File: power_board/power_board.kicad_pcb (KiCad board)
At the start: 2 copper layers, 171.8 x 117.7 mm, 88 parts, among them J1 PROG, J10 M4, J11 5V_1, J12 M5, J13 M6, J14 M7, J15 FAN, J16 Screw_Terminal_01x02, J17 MB_interface, J18 Conn_01x02_Female, J19 12V_1, J2 M1, J20 12V_2, J21 12V_3, J22 12V_4, J23 48V_1, J24 48V_2, J25 48V_3, J26 48V_4, J27 Screw_Terminal_01x02, J3 M2, J4 Conn_01x02_Female, J5 Conn_01x02_Female, J6 Conn_01x01_Male, J7 Conn_01x01_Male, J8 Screw_Terminal_01x02, J9 M3, Q1 2N3906, SW1 SW_Push, U1 ACS758xCB-050B-PFF, U10 MAX31855KASA, U2 ACS758xCB-050B-PFF, U3 MCP2515-EST, U4 MAX31855KASA, U5 ATA6560,1, U6 BTS50085-1TMA, U7 ATmega328P-AU, U8 BTS50085-1TMA, U9 LM2596S-5, Y1 20Mhz, Y2 16Mhz

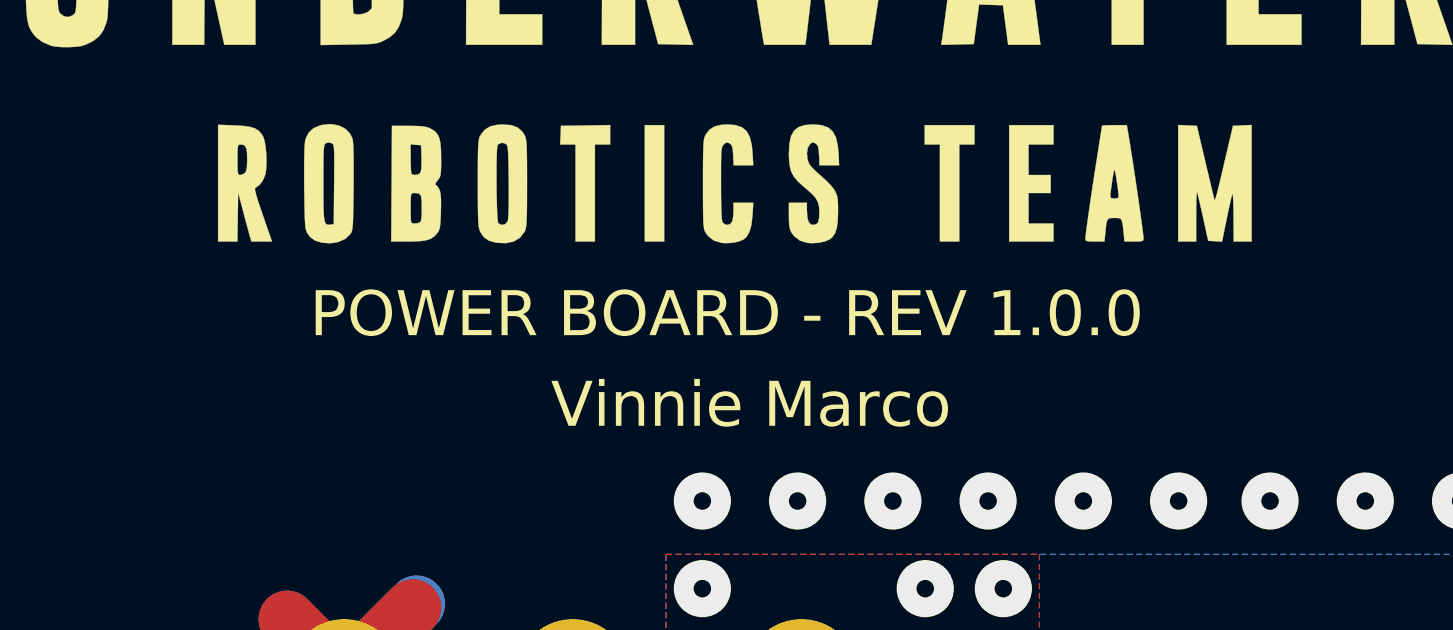
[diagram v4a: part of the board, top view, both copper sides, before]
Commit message: S1.0.0 B1.0.1 Update silkscreen for schematic/pcb version
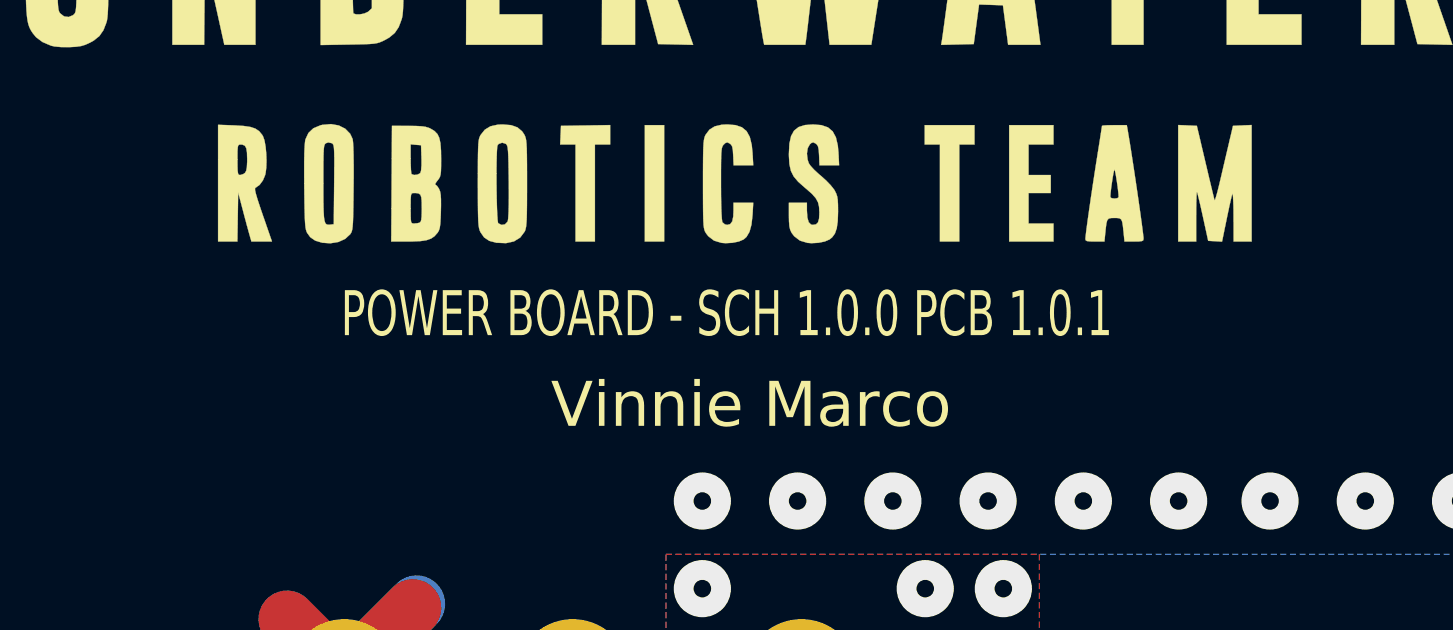
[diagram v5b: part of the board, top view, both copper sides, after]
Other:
- board text added: "POWER BOARD - SCH 1.0.0 PCB 1.0.1"
- board text removed: "POWER BOARD - REV 1.0.0"
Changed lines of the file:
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@@
   )
   (setup
-    (last_trace_width 0.6096)
+    (last_trace_width 0.3048)
     (user_trace_width 0.3048)
     (user_trace_width 0.6096)
@@
       (padsonsilk false)
       (subtractmaskfromsilk false)
-      (outputformat 3)
+      (outputformat 1)
       (mirror false)
       (drillshape 0)
       (scaleselection 1)
-      (outputdirectory "../../../../Desktop/"))
+      (outputdirectory "gerbers_drills/"))
   )
   (net 0 "")
@@
     (effects (font (size 1.5 1.5) (thickness 0.375)))
   )
-  (gr_text "POWER BOARD - REV 1.0.0" (at 157.6578 112.903) (layer F.SilkS)
-    (effects (font (size 1.5 1.5) (thickness 0.375)))
+  (gr_text "POWER BOARD - SCH 1.0.0 PCB 1.0.1" (at 157.6578 112.903) (layer F.SilkS)
+    (effects (font (size 1.5 1) (thickness 0.25)))
   )
   (via (at 152.527 59.563) (size 1.905) (drill 0.5842) (layers F.Cu B.Cu) (net 1))

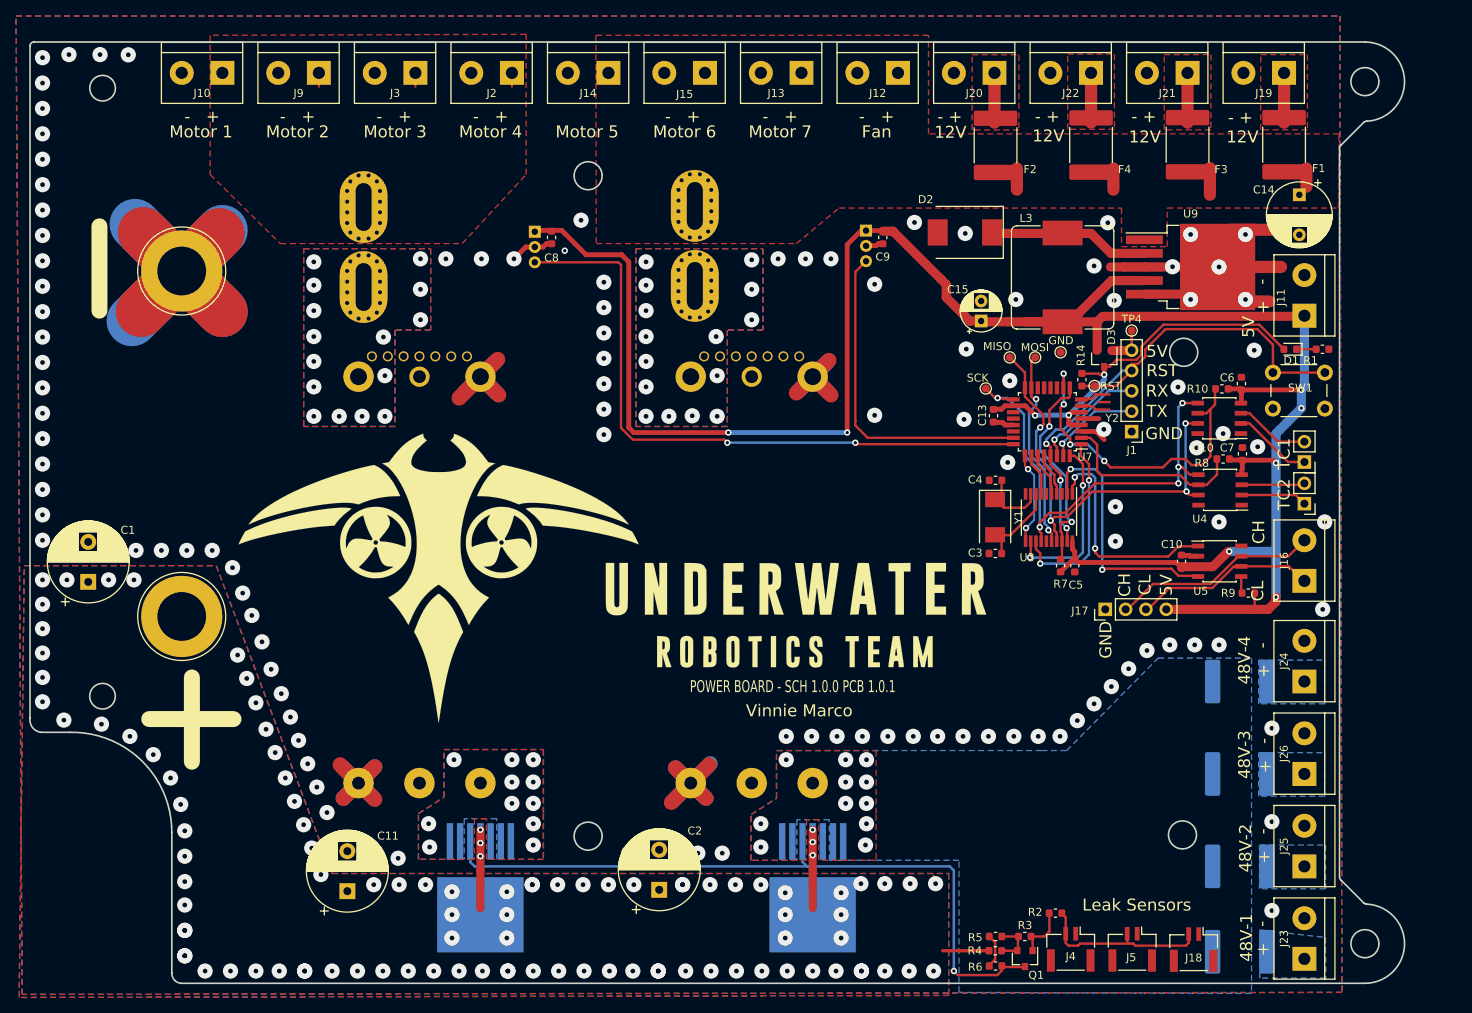
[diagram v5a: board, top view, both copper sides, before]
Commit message: Replaced moutning holes drawn in edge cuts with real holes and regenerated all gerbers
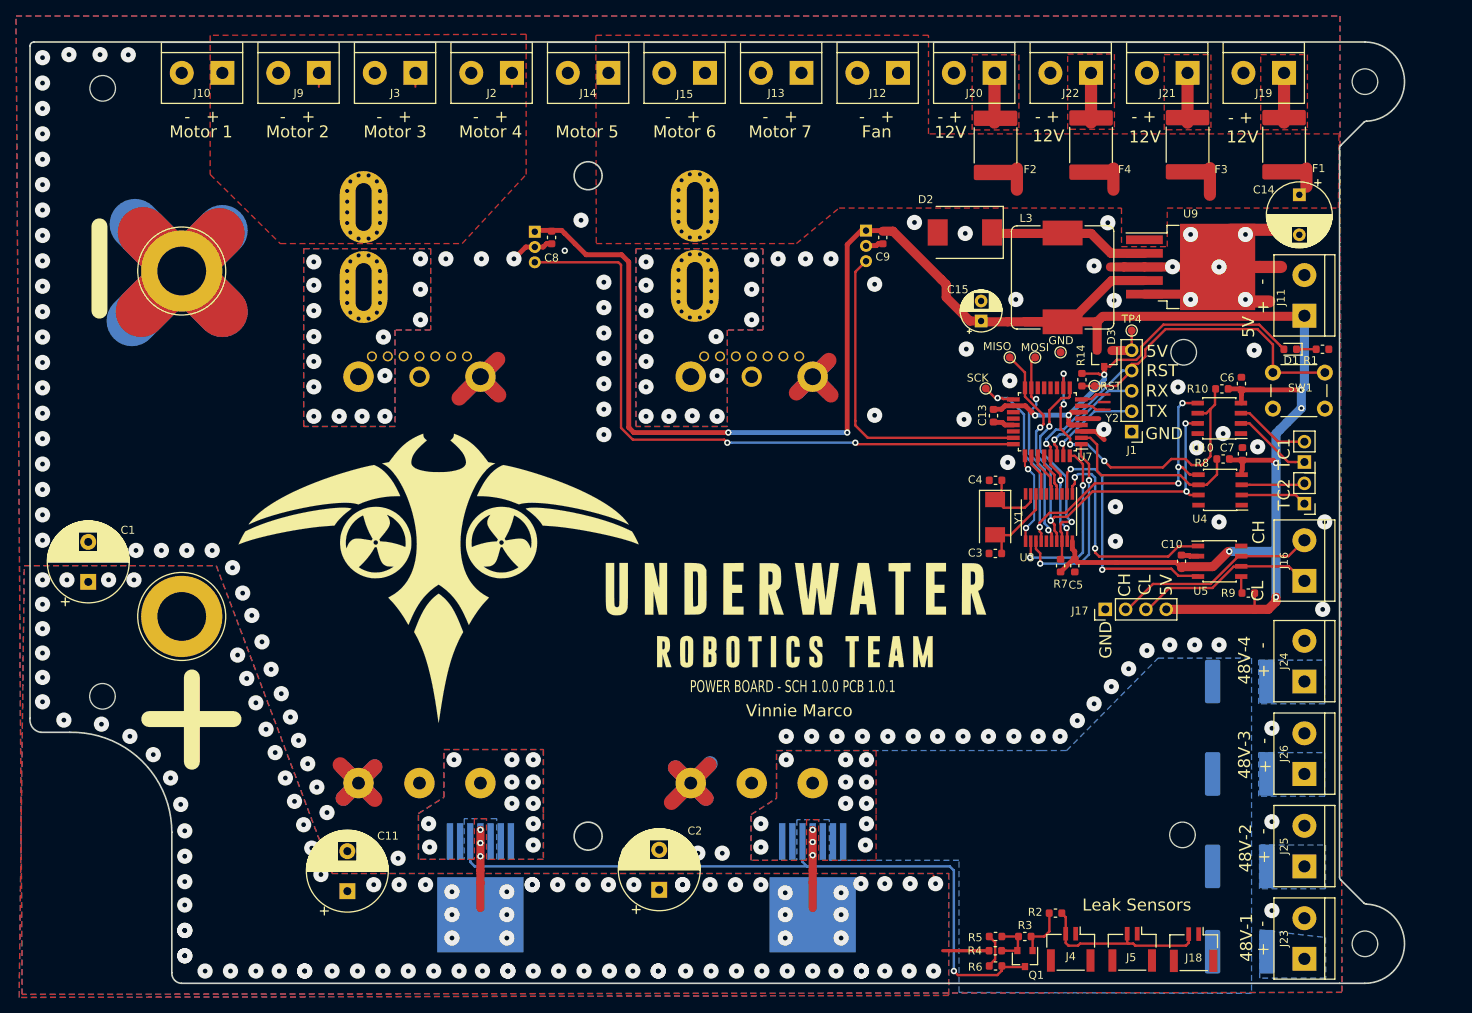
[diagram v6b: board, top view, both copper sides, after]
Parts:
- added REF**: MountingHole_3.2mm_M3, MountingHole:MountingHole_3.2mm_M3, F.Cu at (229.2, 37.3)
- added REF**: MountingHole_3.2mm_M3, MountingHole:MountingHole_3.2mm_M3, F.Cu at (206.5, 71.1)
- added REF**: MountingHole_3.2mm_M3, MountingHole:MountingHole_3.2mm_M3, F.Cu at (206.4, 131.4)
- added REF**: MountingHole_3.2mm_M3, MountingHole:MountingHole_3.2mm_M3, F.Cu at (229.2, 145.1)
- added REF**: MountingHole_3.2mm_M3, MountingHole:MountingHole_3.2mm_M3, F.Cu at (71.4, 114.1)
- added REF**: MountingHole_3.2mm_M3, MountingHole:MountingHole_3.2mm_M3, F.Cu at (71.4, 38.1)
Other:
- outline, holes or cut-outs redrawn
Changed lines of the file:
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@@
   (general
     (thickness 1.6)
-    (drawings 84)
+    (drawings 78)
     (tracks 870)
     (zones 0)
-    (modules 88)
+    (modules 94)
     (nets 69)
   )
@@
       (drillshape 0)
       (scaleselection 1)
-      (outputdirectory "gerbers_drills/"))
+      (outputdirectory "C:/Users/User/Desktop/"))
   )
   (net 0 "")
@@
     (add_net V_MCU)
   )
+  (module MountingHole:MountingHole_3.2mm_M3 (layer F.Cu)
+    (at 229.1842 37.2872)
+    (descr "Mounting Hole 3.2mm, no annular, M3")
+    (tags "mounting hole 3.2mm no annular m3")
+    (attr virtual)
+    (fp_text reference REF** (at 0 -4.2) (layer F.SilkS) hide
+      (effects (font (size 1 1) (thickness 0.15)))
+    )
+    (fp_text value MountingHole_3.2mm_M3 (at 0 4.2) (layer F.Fab)
+      (effects (font (size 1 1) (thickness 0.15)))
+    )
+    (fp_text user %R (at 0.3 0) (layer F.Fab)
+      (effects (font (size 1 1) (thickness 0.15)))
+    )
+    (fp_circle (center 0 0) (end 3.2 0) (layer Cmts.User) (width 0.15))
+    (fp_circle (center 0 0) (end 3.45 0) (layer F.CrtYd) (width 0.05))
+    (pad 1 np_thru_hole circle (at 0 0) (size 3.2 3.2) (drill 3.2) (layers *.Cu *.Mask))
+  )
+  (module MountingHole:MountingHole_3.2mm_M3 (layer F.Cu)
+    (at 206.5274 71.12)
+    (descr "Mounting Hole 3.2mm, no annular, M3")
+    (tags "mounting hole 3.2mm no annular m3")
+    (attr virtual)
+    (fp_text reference REF** (at 0 -4.2) (layer F.SilkS) hide
+      (effects (font (size 1 1) (thickness 0.15)))
+    )
+    (fp_text value MountingHole_3.2mm_M3 (at 0 4.2) (layer F.Fab)
+      (effects (font (size 1 1) (thickness 0.15)))
+    )
+    (fp_circle (center 0 0) (end 3.45 0) (layer F.CrtYd) (width 0.05))
+    (fp_circle (center 0 0) (end 3.2 0) (layer Cmts.User) (width 0.15))
+    (fp_text user %R (at 0.3 0) (layer F.Fab)
+      (effects (font (size 1 1) (thickness 0.15)))
+    )
+    (pad 1 np_thru_hole circle (at 0 0) (size 3.2 3.2) (drill 3.2) (layers *.Cu *.Mask))
+  )
+  (module MountingHole:MountingHole_3.2mm_M3 (layer F.Cu)
+    (at 206.375 131.445)
+    (descr "Mounting Hole 3.2mm, no annular, M3")
+    (tags "mounting hole 3.2mm no annular m3")
+    (attr virtual)
+    (fp_text reference REF** (at 0 -4.2) (layer F.SilkS) hide
+      (effects (font (size 1 1) (thickness 0.15)))
+    )
+    (fp_text value MountingHole_3.2mm_M3 (at 0 4.2) (layer F.Fab)
+      (effects (font (size 1 1) (thickness 0.15)))
+    )
+    (fp_text user %R (at 0.3 0) (layer F.Fab)
+      (effects (font (size 1 1) (thickness 0.15)))
+    )
+    (fp_circle (center 0 0) (end 3.2 0) (layer Cmts.User) (width 0.15))
+    (fp_circle (center 0 0) (end 3.45 0) (layer F.CrtYd) (width 0.05))
+    (pad 1 np_thru_hole circle (at 0 0) (size 3.2 3.2) (drill 3.2) (layers *.Cu *.Mask))
+  )
+  (module MountingHole:MountingHole_3.2mm_M3 (layer F.Cu)
+    (at 229.1842 145.0594)
+    (descr "Mounting Hole 3.2mm, no annular, M3")
+    (tags "mounting hole 3.2mm no annular m3")
+    (attr virtual)
+    (fp_text reference REF** (at 0 -4.2) (layer F.SilkS) hide
+      (effects (font (size 1 1) (thickness 0.15)))
+    )
+    (fp_text value MountingHole_3.2mm_M3 (at 0 4.2) (layer F.Fab)
+      (effects (font (size 1 1) (thickness 0.15)))
+    )
+    (fp_circle (center 0 0) (end 3.45 0) (layer F.CrtYd) (width 0.05))
+    (fp_circle (center 0 0) (end 3.2 0) (layer Cmts.User) (width 0.15))
+    (fp_text user %R (at 0.3 0) (layer F.Fab)
+      (effects (font (size 1 1) (thickness 0.15)))
+    )
+    (pad 1 np_thru_hole circle (at 0 0) (size 3.2 3.2) (drill 3.2) (layers *.Cu *.Mask))
+  )
+  (module MountingHole:MountingHole_3.2mm_M3 (layer F.Cu)
+    (at 71.374 114.1222)
+    (descr "Mounting Hole 3.2mm, no annular, M3")
+    (tags "mounting hole 3.2mm no annular m3")
+    (attr virtual)
+    (fp_text reference REF** (at 0 -4.2) (layer F.SilkS) hide
+      (effects (font (size 1 1) (thickness 0.15)))
+    )
+    (fp_text value MountingHole_3.2mm_M3 (at 0 4.2) (layer F.Fab)
+      (effects (font (size 1 1) (thickness 0.15)))
+    )
+    (fp_text user %R (at 0.3 0) (layer F.Fab)
+      (effects (font (size 1 1) (thickness 0.15)))
+    )
+    (fp_circle (center 0 0) (end 3.2 0) (layer Cmts.User) (width 0.15))
+    (fp_circle (center 0 0) (end 3.45 0) (layer F.CrtYd) (width 0.05))
+    (pad 1 np_thru_hole circle (at 0 0) (size 3.2 3.2) (drill 3.2) (layers *.Cu *.Mask))
+  )
   (module Diode_SMD:D_SMC (layer F.Cu)
     (at 179.1752 56.134 180)
@@
       (xy -13.727278 2.362363) (xy -13.654921 2.345019) (xy -13.369211 2.320423) (xy -13.110773 2.36591)) (layer F.SilkS) (width 0.01))
   )
+  (module MountingHole:MountingHole_3.2mm_M3 (layer F.Cu)
+    (at 71.3994 38.1254)
+    (descr "Mounting Hole 3.2mm, no annular, M3")
+    (tags "mounting hole 3.2mm no annular m3")
+    (attr virtual)
+    (fp_text reference REF** (at 0 -4.2) (layer F.SilkS) hide
+      (effects (font (size 1 1) (thickness 0.15)))
+    )
+    (fp_text value MountingHole_3.2mm_M3 (at 0 4.2) (layer F.Fab)
+      (effects (font (size 1 1) (thickness 0.15)))
+    )
+    (fp_circle (center 0 0) (end 3.45 0) (layer F.CrtYd) (width 0.05))
+    (fp_circle (center 0 0) (end 3.2 0) (layer Cmts.User) (width 0.15))
+    (fp_text user %R (at 0.3 0) (layer F.Fab)
+      (effects (font (size 1 1) (thickness 0.15)))
+    )
+    (pad 1 np_thru_hole circle (at 0 0) (size 3.2 3.2) (drill 3.2) (layers *.Cu *.Mask))
+  )
   (gr_text SCK (at 180.7718 74.3204) (layer F.SilkS)
     (effects (font (size 1 1) (thickness 0.15)))
@@
     (effects (font (size 1 1) (thickness 0.15)))
   )
-  (gr_circle (center 206.375 131.445) (end 208.125 131.445) (layer Edge.Cuts) (width 0.2))
-  (gr_circle (center 206.53 71.12) (end 208.28 71.12) (layer Edge.Cuts) (width 0.2))
   (gr_circle (center 132.08 49.05) (end 133.83 49.05) (layer Edge.Cuts) (width 0.2))
   (gr_circle (center 132.08 131.6) (end 133.83 131.6) (layer Edge.Cuts) (width 0.2))
@@
     (effects (font (size 1.5 1.5) (thickness 0.375)))
   )
-  (gr_circle (center 229.180248 37.285694) (end 230.930248 37.285694) (layer Edge.Cuts) (width 0.2))
   (gr_arc (start 63.869585 117.072557) (end 62.318197 116.888994) (angle -90) (layer Edge.Cuts) (width 0.2))
   (gr_arc (start 229.180248 145.04529) (end 229.180248 149.998194) (angle -177.7803021) (layer Edge.Cuts) (width 0.2))
@@
   (gr_line (start 226.005248 136.710279) (end 226.005248 45.620705) (layer Edge.Cuts) (width 0.2))
   (gr_line (start 229.037892 139.950031) (end 226.151694 137.063832) (layer Edge.Cuts) (width 0.2))
-  (gr_circle (center 229.180248 145.04529) (end 230.930248 145.04529) (layer Edge.Cuts) (width 0.2))
   (gr_arc (start 67.555997 131.109174) (end 80.043854 131.109174) (angle -91.17565039) (layer Edge.Cuts) (width 0.2))
-  (gr_circle (center 71.38887 38.107527) (end 69.78887 38.107527) (layer Edge.Cuts) (width 0.2))
-  (gr_circle (center 71.377739 114.108975) (end 69.777739 114.108975) (layer Edge.Cuts) (width 0.2))
   (gr_text "Vinnie Marco" (at 158.4706 115.9256) (layer F.SilkS)
     (effects (font (size 1.5 1.5) (thickness 0.3)))

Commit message: selected new footprint for BJT for power shutoff
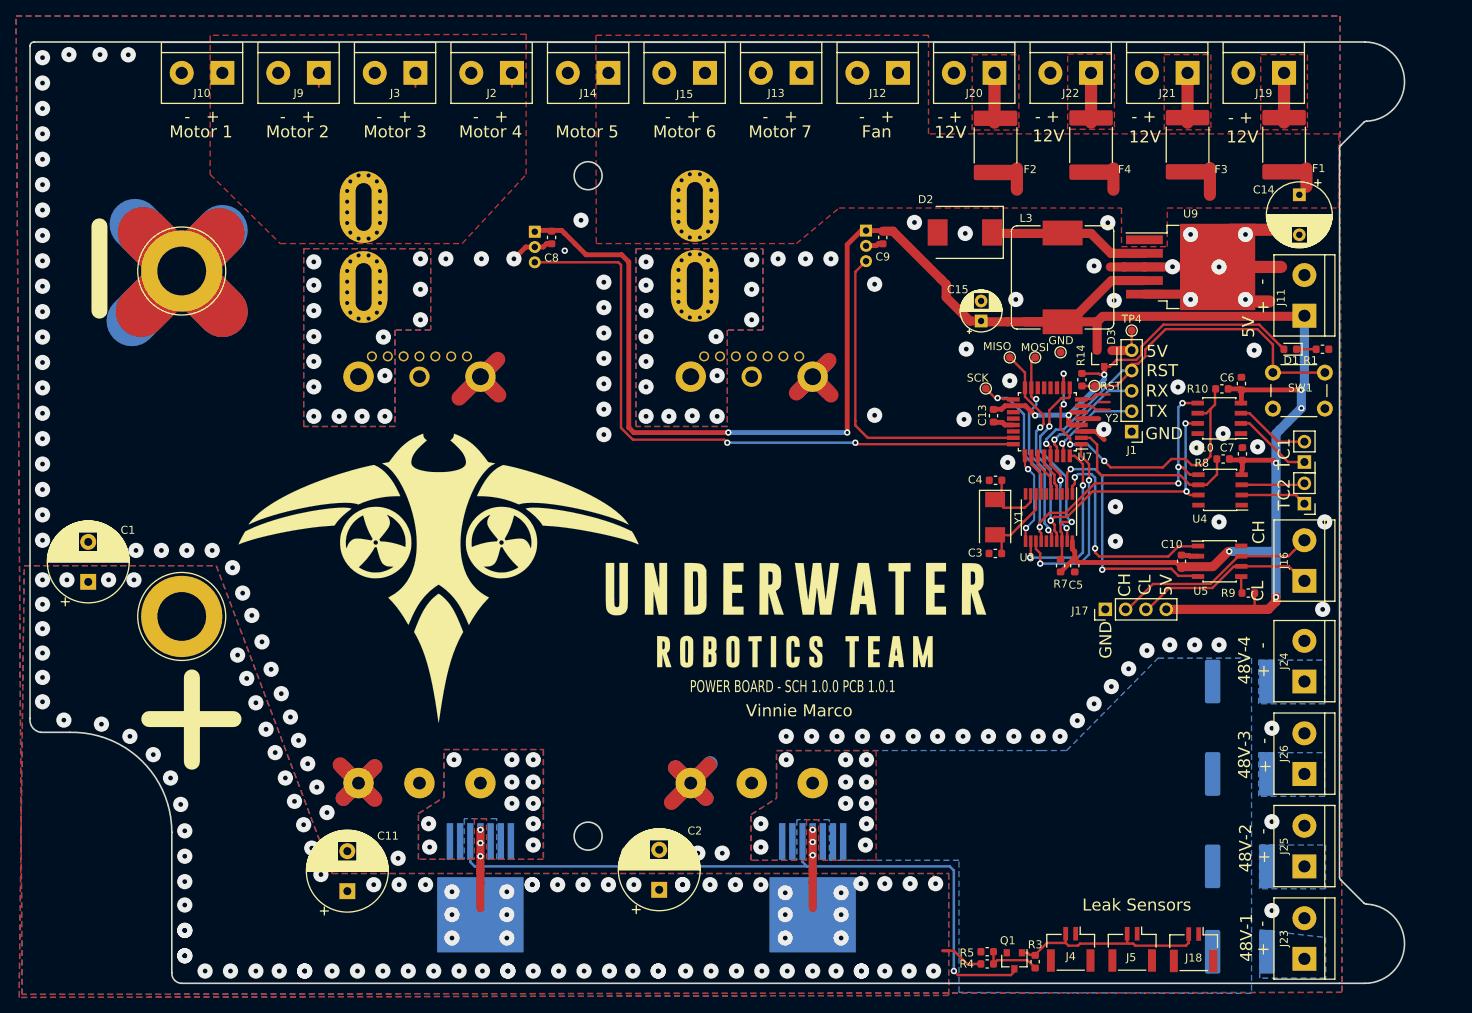
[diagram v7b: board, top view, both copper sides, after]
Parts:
- removed R2: 1k, Resistor_SMD:R_0603_1608Metric
- removed R6: 10k, Resistor_SMD:R_0603_1608Metric
- removed REF** (x6): MountingHole_3.2mm_M3, MountingHole:MountingHole_3.2mm_M3
- Q1: value 2N3906 -> Q_NPN_BEC
- moved R3 3.41 mm to (188.0, 147.3), turned to 270 degrees
- moved R5 2.17 mm to (182.0, 146.1)
- moved R4 1.94 mm to (182.0, 147.6)
- moved Q1 1.36 mm to (185.4, 147.2)
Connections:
- Q1 pad 1: Net-(Q1-Pad1) -> Net-(J18-Pad2)
- Q1 pad 2: +5VA -> GNDREF
- R3 pad 1: Net-(Q1-Pad1) -> Net-(J18-Pad2)
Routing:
- net Net-(Q1-Pad1): track 6.92 -> 0.00 mm
- net GNDREF: track 202.8 -> 198.5 mm
- net Net-(J18-Pad2): track 22.2 -> 25.6 mm
- net SHUTOFF: track 89.6 -> 87.9 mm
- net +5VA: track 6.10 -> 7.32 mm
